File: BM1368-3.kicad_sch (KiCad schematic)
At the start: 39 parts, among them U14 BM1368_mode1, U15 BM1368_mode1

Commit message: Added 4th Phase Buck
Started to add 4th Phase for the Buck, implementing BM1370 footprint etc
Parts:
- removed U14, U15: BM1368_mode1, myfootprints:bm1368-package-modified, symbol mylib7:BM1368_mode1
- added U13, U14: BM1370_mode1, Nerd8:BM1370, symbol bitaxe:BM1370_mode1
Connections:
- net +0V8: now also U13.14 (VDDIO_08_0), U13.17 (VDDIO_08_1), U14.14 (VDDIO_08_0), U14.17 (VDDIO_08_1)
- net +1V2: now also U13.31 (VDD), U14.31 (VDD)
- net +1V8: now also U13.15 (VDDIO_12_0), U13.16 (VDDIO_12_1), U14.15 (VDDIO_12_0), U14.16 (VDDIO_12_1)
- net BI: now also U13.9 (BI)
- net CI: now also U13.6 (CI)
- net CLKI: now also U13.8 (CLKI)
- net GND: now also U13.13 (PLL_VSS), U13.18 (VSS), U13.27 (VSS), U13.32 (VSS), U13.4 (VSS), U14.13 (PLL_VSS), U14.18 (VSS), U14.27 (VSS), U14.32 (VSS), U14.4 (VSS)
- net NRSTI: now also U13.5 (NRSTI)
- net RI: now also U14.24 (RI)
- net RO: now also U13.7 (RO)
- net U13-VDD1_1: now also U13.3 (VDD1_0)
- net U13-VDD2_1: now also U13.2 (VDD2_0)
- net U13-VDD3_1: now also U13.1 (VDD3_0)
- net at C161.2, C164.1, C171.1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: now also U13.30 (VDD3_1), U14.1 (VDD3_0)
- net at C164.2, C166.1, C220.2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: now also U13.29 (VDD2_1), U14.2 (VDD2_0)
- net at C166.2, C169.1, C219.2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: now also U13.28 (VDD1_1), U14.3 (VDD1_0)
- net at C174.2, C175.1: now also U14.28 (VDD1_1)
- net at R45.1: now also U14.11 (LITE_PAD)
- net at C173.2, C174.1: now also U14.29 (VDD2_1)
- net at C172.2, C173.1: now also U14.30 (VDD3_1)
- net at R44.2: now also U13.26 (NRSTO), U14.5 (NRSTI)
- net at R43.1: now also U13.24 (RI), U14.7 (RO)
- net at R42.1: now also U13.11 (LITE_PAD)
- new net: U13.22 (BO), U14.9 (BI)
- new net: U13.23 (CLKO), U14.8 (CLKI)
- new net: U13.25 (CO), U14.6 (CI)

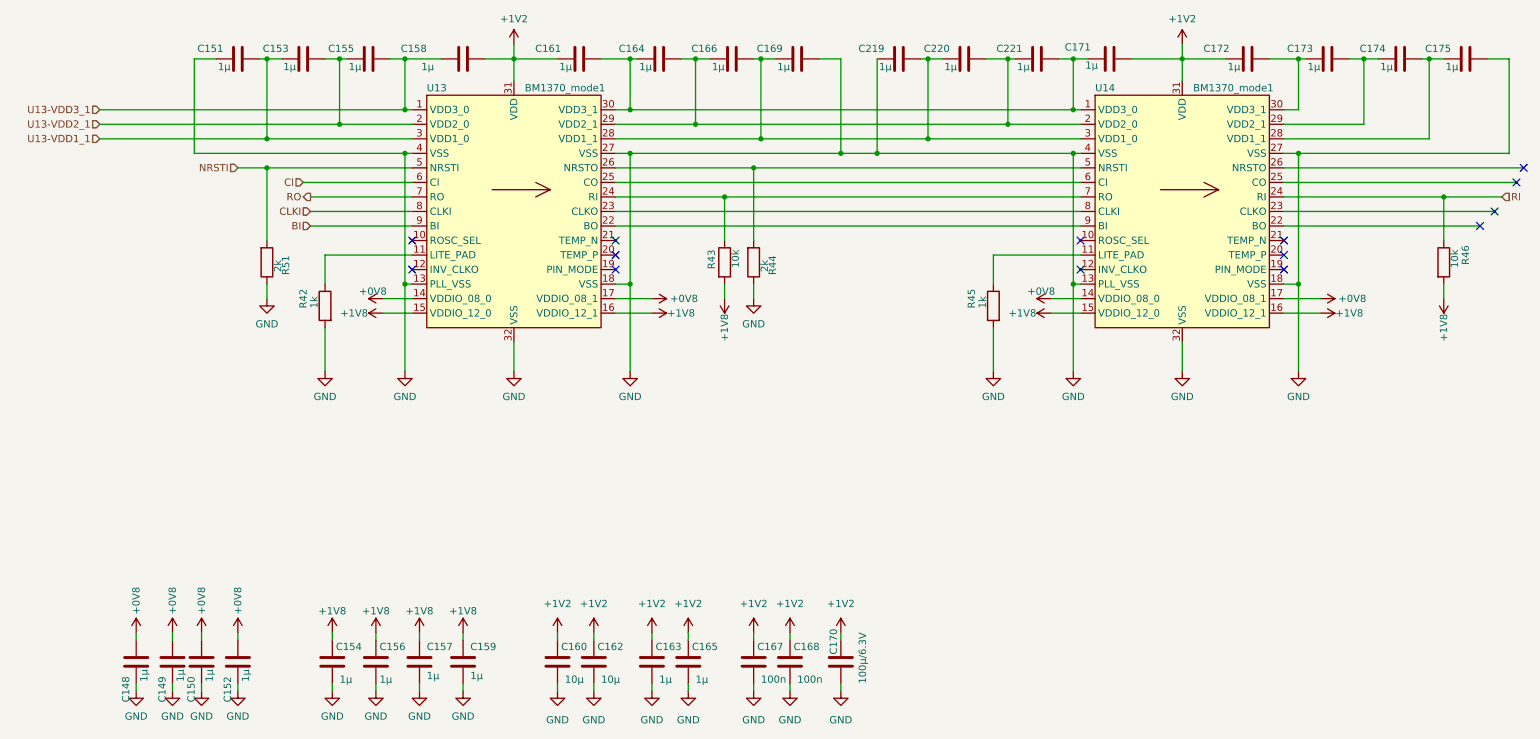
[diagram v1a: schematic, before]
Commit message: Changed LDO to 1V2 and original 1V2 to VDD
1V8 LDO replaced with 1V2 LDO
Crystal replaced
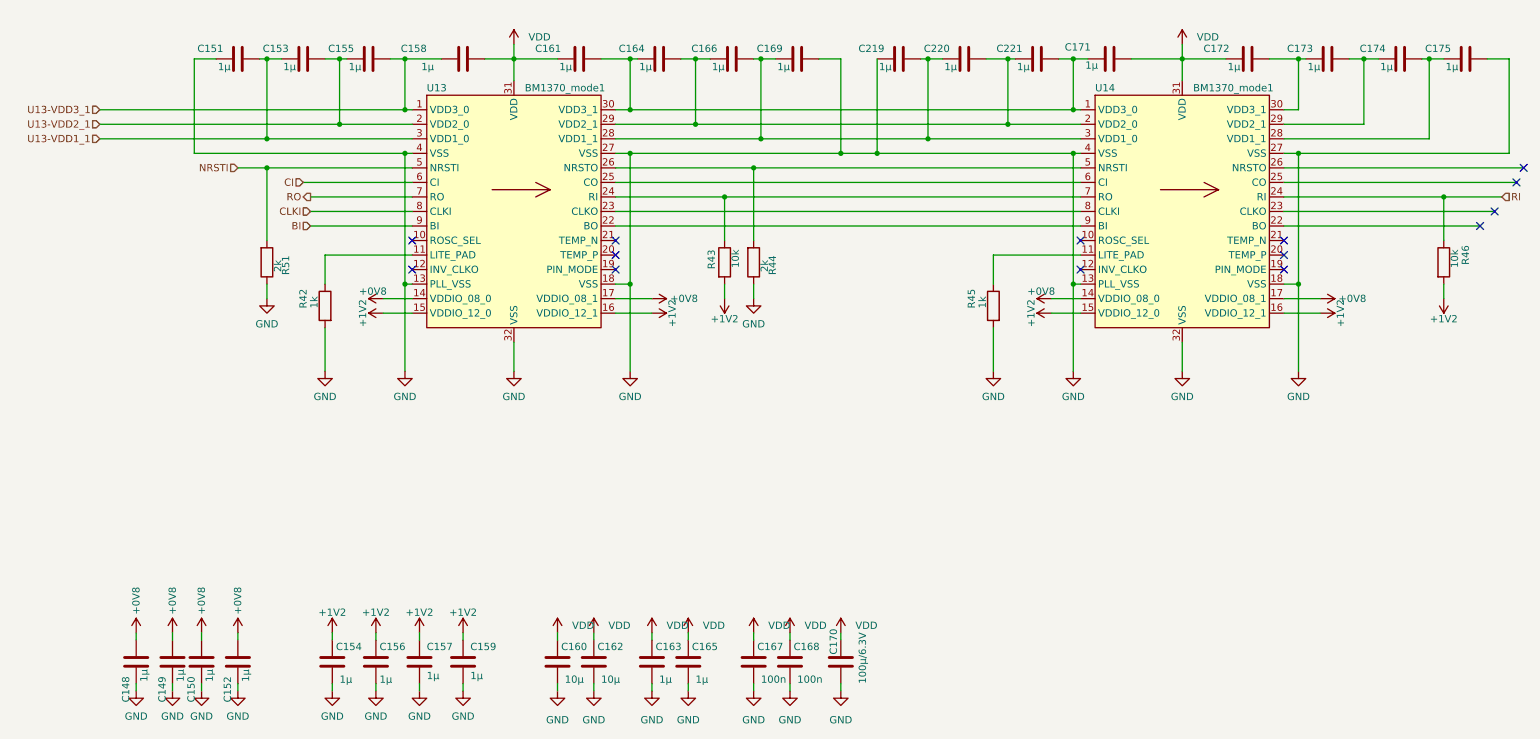
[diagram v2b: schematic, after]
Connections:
- net +1V8 is gone; now on net +1V2: C154.1, C156.1, C157.1, C159.1, R43.2, R46.2, U13.15 (VDDIO_12_0), U13.16 (VDDIO_12_1), U14.15 (VDDIO_12_0), U14.16 (VDDIO_12_1)
- net +1V2: no longer C158.2, C160.1, C161.1, C162.1, C163.1, C165.1, C167.1, C168.1, C170.1, C171.2, C172.1, U13.31 (VDD), U14.31 (VDD)
- new net VDD: C158.2, C160.1, C161.1, C162.1, C163.1, C165.1, C167.1, C168.1, C170.1, C171.2, C172.1, U13.31 (VDD), U14.31 (VDD)

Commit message: BOM changes
1nF  to 1nF 0.7mm etc
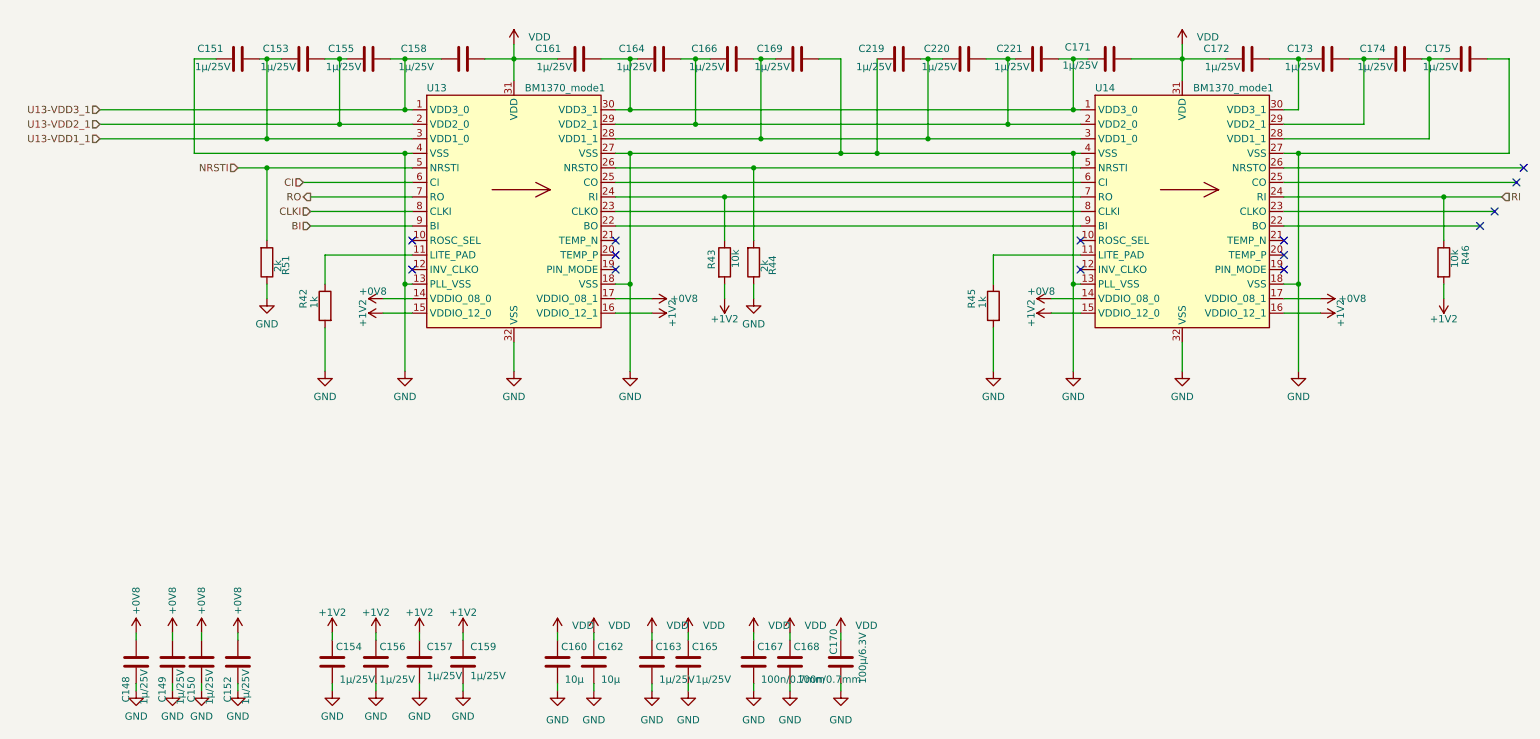
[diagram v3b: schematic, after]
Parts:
- C148, C149, C150, C151, C152, C153, C154, C155, C156, C157, C158, C159, C161, C163, C164, C165, C166, C169, C171, C172, C173, C174, C175, C219, C220, C221: value 1µ -> 1µ/25V; Distributor (none) -> D; Manufacturer (none) -> CL21B105KAFNNNE; OrderNr (none) -> 1276-1066-1-ND
- C167, C168: value 100n -> 100n/0.7mm; Distributor (none) -> D; Manufacturer (none) -> AC0805KRX7R9BB104; OrderNr (none) -> 311-3037-1-ND
- R42, R45: Distributor (none) -> D; Manufacturer (none) -> RNCP0805FTD1K00; OrderNr (none) -> RNCP0805FTD1K00CT-ND
- R43, R46: Distributor (none) -> D; Manufacturer (none) -> RMCF0805FT10K0; OrderNr (none) -> RMCF0805FT10K0CT-ND
- R44, R51: Distributor (none) -> D; Manufacturer (none) -> CRG0805F2K0; OrderNr (none) -> A126358CT-ND
- U13, U14: Manufacturer (none) -> BM1370 BITMAIN; OrderNr (none) -> -
